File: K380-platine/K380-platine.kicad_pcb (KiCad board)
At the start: 2 copper layers, 98 x 35 mm, 0 parts

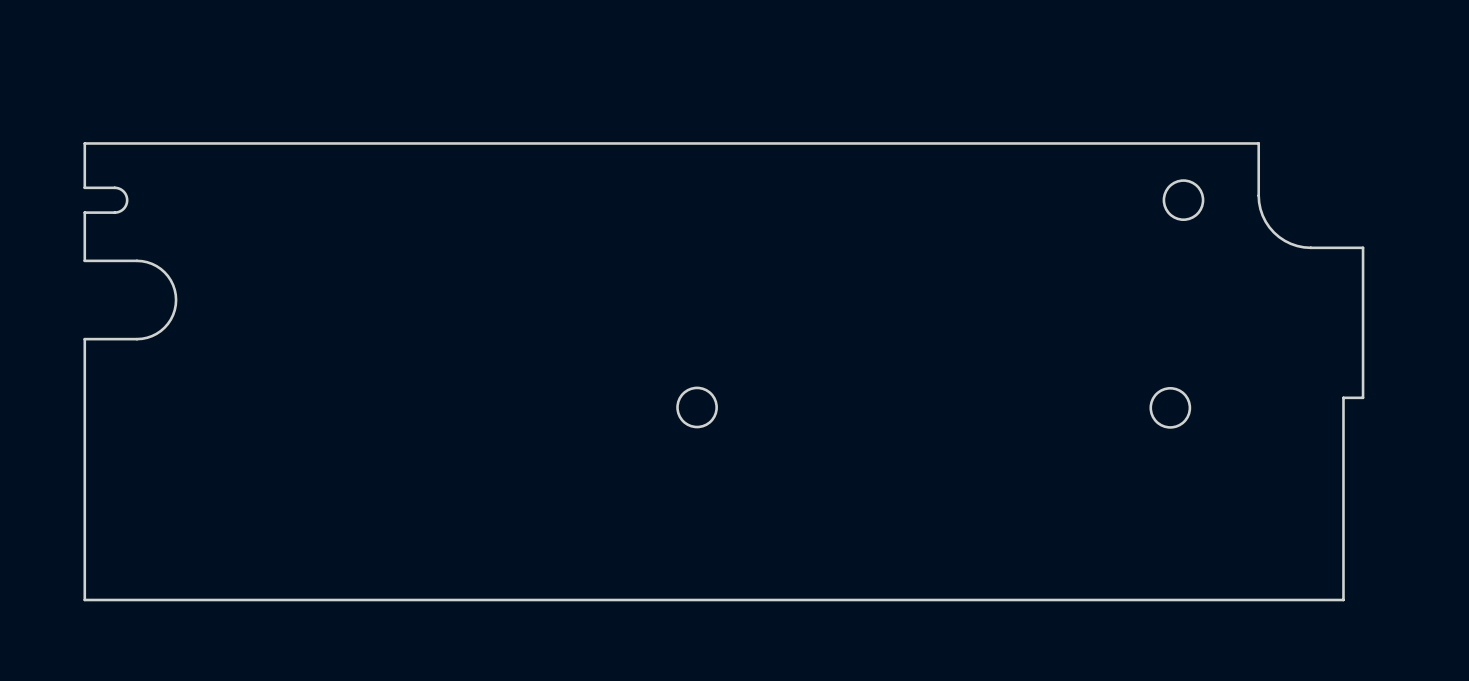
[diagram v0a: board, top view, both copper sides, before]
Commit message: Add few major components
- completely unconnected
- created schematic for M.2 sparkfun nRF52840 module
- included SparkFun footprint library
- position a few major components on the footprint
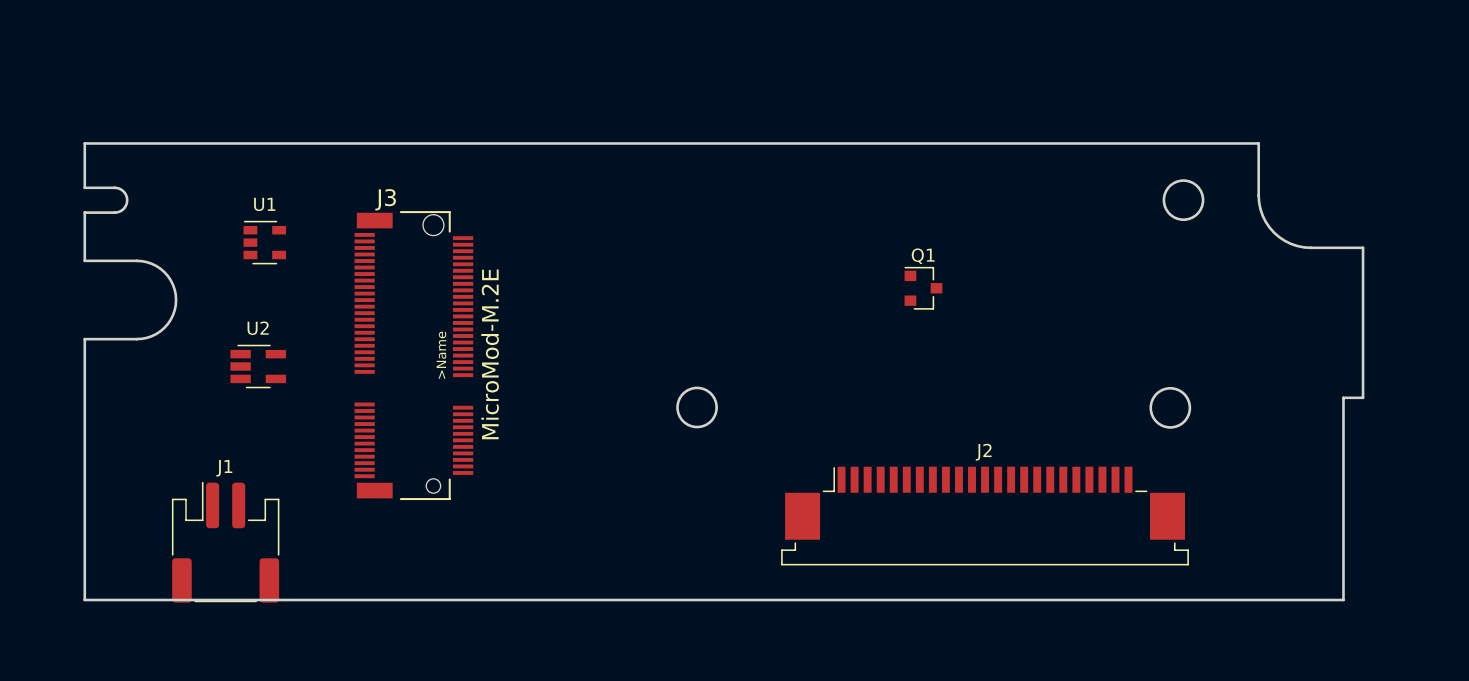
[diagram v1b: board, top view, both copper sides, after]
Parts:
- added J1: JST-PH 2, Connector_JST:JST_PH_S2B-PH-SM4-TB_1x02-1MP_P2.00mm_Horizontal, F.Cu at (86.5, 96.0)
- added J2: Conn_01x23, Connector_FFC-FPC:TE_2-84952-3_1x23-1MP_P1.0mm_Horizontal, F.Cu at (144.7, 93.0)
- added J3: MicroMod-M.2E, SparkFun MicroMod:M.2-CONNECTOR-E, F.Cu at (102.4, 81.7)
- added Q1: PMost Enc FET -20V, Package_TO_SOT_SMD:SOT-23, F.Cu at (140.0, 76.5)
- added U1: XC6220B331MR, Package_TO_SOT_SMD:SOT-23-5, F.Cu at (89.5, 73.0)
- added U2: MCP73831-2-OT, Package_TO_SOT_SMD:SOT-23-5_HandSoldering, F.Cu at (89.0, 82.5)

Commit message: Basic sorting of components on footprint
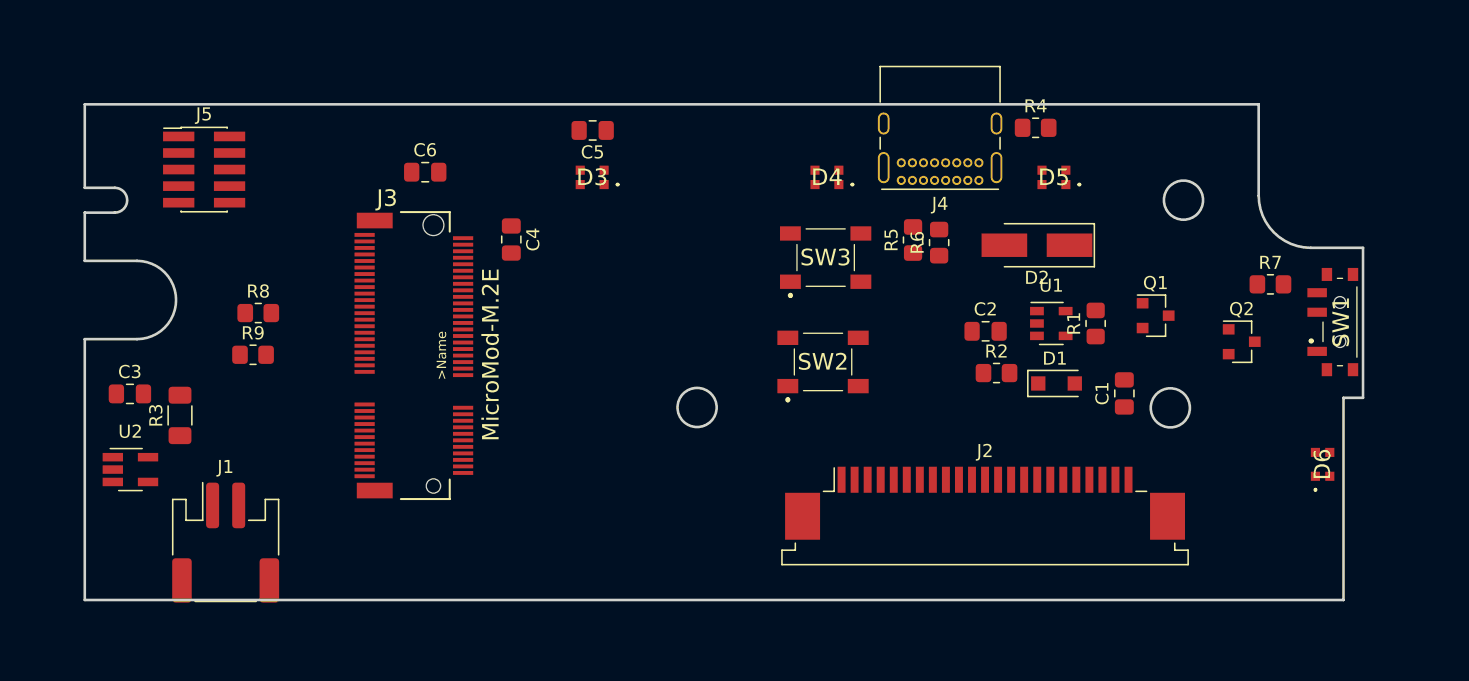
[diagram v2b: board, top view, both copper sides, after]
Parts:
- added C1: 10uF, Capacitor_SMD:C_0805_2012Metric_Pad1.18x1.45mm_HandSolder, F.Cu at (155.4, 84.6)
- added C2: 4.7uF, Capacitor_SMD:C_0805_2012Metric_Pad1.18x1.45mm_HandSolder, F.Cu at (144.8, 79.8)
- added C3: 10uF, Capacitor_SMD:C_0805_2012Metric_Pad1.18x1.45mm_HandSolder, F.Cu at (79.2, 84.6)
- added C4: 10uF, Capacitor_SMD:C_0805_2012Metric_Pad1.18x1.45mm_HandSolder, F.Cu at (108.4, 72.8)
- added C5: 0.1uF, Capacitor_SMD:C_0805_2012Metric_Pad1.18x1.45mm_HandSolder, F.Cu at (114.6, 64.4)
- added C6: 0.1uF, Capacitor_SMD:C_0805_2012Metric_Pad1.18x1.45mm_HandSolder, F.Cu at (101.8, 67.6)
- added D1: MBR1020VL, Diode_SMD:D_SOD-123F, F.Cu at (150.2, 83.8)
- added D2: TVS 5V, Diode_SMD:D_SMA_Handsoldering, F.Cu at (148.7, 73.2)
- added D3: WS2812B, LibraryLoader:WS28122020, F.Cu at (114.6, 68.0)
- added D4: WS2812B, LibraryLoader:WS28122020, F.Cu at (132.6, 68.0)
- added D5: WS2812B, LibraryLoader:WS28122020, F.Cu at (150.0, 68.0)
- added D6: WS2812B, LibraryLoader:WS28122020, F.Cu at (170.6, 90.0)
- added J4: USB_C_Receptacle_USB2.0, Connector_USB:USB_C_Receptacle_GCT_USB4085, F.Cu at (144.2, 68.2)
- added J5: Conn_ARM_JTAG_SWD_10, Connector_PinHeader_1.27mm:PinHeader_2x05_P1.27mm_Vertical_SMD, F.Cu at (84.8, 67.4)
- added Q2: Q_NMOS_DGS, Package_TO_SOT_SMD:SOT-23, F.Cu at (164.4, 80.6)
- added R1: 100K, Resistor_SMD:R_0805_2012Metric_Pad1.20x1.40mm_HandSolder, F.Cu at (153.2, 79.2)
- added R2: 100K, Resistor_SMD:R_0805_2012Metric_Pad1.20x1.40mm_HandSolder, F.Cu at (145.6, 83.0)
- added R3: RProg, Resistor_SMD:R_1206_3216Metric_Pad1.30x1.75mm_HandSolder, F.Cu at (83.0, 86.2)
- added R4: 1M, Resistor_SMD:R_0805_2012Metric_Pad1.20x1.40mm_HandSolder, F.Cu at (148.6, 64.2)
- added R5: 5.1k 20%, Resistor_SMD:R_0805_2012Metric_Pad1.20x1.40mm_HandSolder, F.Cu at (139.2, 72.8)
- added R6: 5.1k 20%, Resistor_SMD:R_0805_2012Metric_Pad1.20x1.40mm_HandSolder, F.Cu at (141.2, 73.0)
- added R7: 100K, Resistor_SMD:R_0805_2012Metric_Pad1.20x1.40mm_HandSolder, F.Cu at (166.6, 76.2)
- added R8: 100K, Resistor_SMD:R_0805_2012Metric_Pad1.20x1.40mm_HandSolder, F.Cu at (89.0, 78.4)
- added R9: 100K, Resistor_SMD:R_0805_2012Metric_Pad1.20x1.40mm_HandSolder, F.Cu at (88.6, 81.6)
- added SW1: EG1215AA, LibraryLoader:EG1215AA, F.Cu at (171.9, 79.1)
- added SW2: SW_Push, LibraryLoader:MJTP1140AAUTR, F.Cu at (132.3, 82.2)
- added SW3: SW_Push, LibraryLoader:MJTP1140AAUTR, F.Cu at (132.5, 74.2)
- moved U1 60.6 mm to (149.8, 79.2)
- moved Q1 17.9 mm to (157.8, 78.6)
- moved U2 12.6 mm to (79.2, 90.4)
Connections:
- net Net-(J3-Pad13) renamed CSTAT
- net Net-(U2-Pad1) renamed CStat
- J1 pad 1: Net-(J1-Pad1) -> GND
- J1 pad 2: Net-(J1-Pad2) -> VBAT
- J2 pad 1: Net-(J2-Pad1) -> COL1
- J2 pad 10: Net-(J2-Pad10) -> COL2
- J2 pad 11: Net-(J2-Pad11) -> COL3
- J2 pad 12: Net-(J2-Pad12) -> COL4
- J2 pad 13: Net-(J2-Pad13) -> COL5
- J2 pad 14: Net-(J2-Pad14) -> COL6
- J2 pad 15: Net-(J2-Pad15) -> COL7
- J2 pad 16: Net-(J2-Pad16) -> COL8
- J2 pad 17: Net-(J2-Pad17) -> COL9
- J2 pad 18: Net-(J2-Pad18) -> COL10
- J2 pad 19: Net-(J2-Pad19) -> COL11
- J2 pad 2: Net-(J2-Pad2) -> ROW1
- J2 pad 20: Net-(J2-Pad20) -> COL12
- J2 pad 21: Net-(J2-Pad21) -> COL13
- J2 pad 22: Net-(J2-Pad22) -> COL14
- J2 pad 23: Net-(J2-Pad23) -> COL15
- J2 pad 3: Net-(J2-Pad3) -> ROW2
- J2 pad 4: Net-(J2-Pad4) -> ROW3
- J2 pad 5: Net-(J2-Pad5) -> ROW4
- J2 pad 6: Net-(J2-Pad6) -> ROW5
- J2 pad 7: Net-(J2-Pad7) -> ROW6
- J2 pad 8: Net-(J2-Pad8) -> ROW7
- J2 pad 9: Net-(J2-Pad9) -> ROW8
- J3 pad 1: Net-(J3-Pad1) -> GND
- J3 pad 10: Net-(J3-Pad10) -> COL13
- J3 pad 11: Net-(J3-Pad11) -> BOOT
- J3 pad 12: Net-(J3-Pad12) -> COL2
- J3 pad 14: Net-(J3-Pad14) -> COL5
- J3 pad 15: Net-(J3-Pad15) -> ROW6
- J3 pad 16: Net-(J3-Pad16) -> COL6
- J3 pad 18: Net-(J3-Pad18) -> ROW5
- J3 pad 19: Net-(J3-Pad19) -> ROW7
- J3 pad 2: Net-(J3-Pad2) -> V3.3
- J3 pad 20: Net-(J3-Pad20) -> ROW2
- J3 pad 21: Net-(J3-Pad21) -> SWDCLK
- J3 pad 22: Net-(J3-Pad22) -> ROW4
- J3 pad 23: Net-(J3-Pad23) -> SWDIO
- J3 pad 3: Net-(J3-Pad3) -> D+
- J3 pad 32: Net-(J3-Pad32) -> COL1
- J3 pad 33: Net-(J3-Pad33) -> GND
- J3 pad 36: Net-(J3-Pad36) -> GND
- J3 pad 39: Net-(J3-Pad39) -> GND
- J3 pad 4: Net-(J3-Pad4) -> V3.3
- J3 pad 40: Net-(J3-Pad40) -> COL15
- J3 pad 45: Net-(J3-Pad45) -> GND
- J3 pad 47: Net-(J3-Pad47) -> COL7
- J3 pad 48: Net-(J3-Pad48) -> ROW8
- J3 pad 5: Net-(J3-Pad5) -> D-
- J3 pad 50: Net-(J3-Pad50) -> COL11
- J3 pad 51: Net-(J3-Pad51) -> DLED
- J3 pad 52: Net-(J3-Pad52) -> COL12
- J3 pad 53: Net-(J3-Pad53) -> COL10
- J3 pad 55: Net-(J3-Pad55) -> COL9
- J3 pad 57: Net-(J3-Pad57) -> COL14
- J3 pad 6: Net-(J3-Pad6) -> RESET
- J3 pad 61: Net-(J3-Pad61) -> VDIV
- J3 pad 63: Net-(J3-Pad63) -> COL4
- J3 pad 65: Net-(J3-Pad65) -> COL3
- J3 pad 69: Net-(J3-Pad69) -> ROW1
- J3 pad 7: Net-(J3-Pad7) -> GND
- J3 pad 71: Net-(J3-Pad71) -> ROW3
- J3 pad 73: Net-(J3-Pad73) -> COL8
- J3 pad 74: Net-(J3-Pad74) -> V3.3
- J3 pad 75: Net-(J3-Pad75) -> GND
- J3 pad 9: Net-(J3-Pad9) -> VUSB
- Q1 pad 1: Net-(Q1-Pad1) -> VUSB
- Q1 pad 2: Net-(Q1-Pad2) -> Net-(C1-Pad1)
- U1 pad 1: Net-(U1-Pad1) -> Net-(C1-Pad1)
- U1 pad 2: Net-(U1-Pad2) -> GND
- U1 pad 5: Net-(U1-Pad5) -> V3.3
- U2 pad 2: Net-(U2-Pad2) -> GND
- U2 pad 3: Net-(U2-Pad3) -> VBAT
- U2 pad 4: Net-(U2-Pad4) -> VUSB
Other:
- board size 98 x 35 mm -> 98 x 38 mm

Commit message: Reordered keyboard matrix pins
- layout traces isn't as random as before
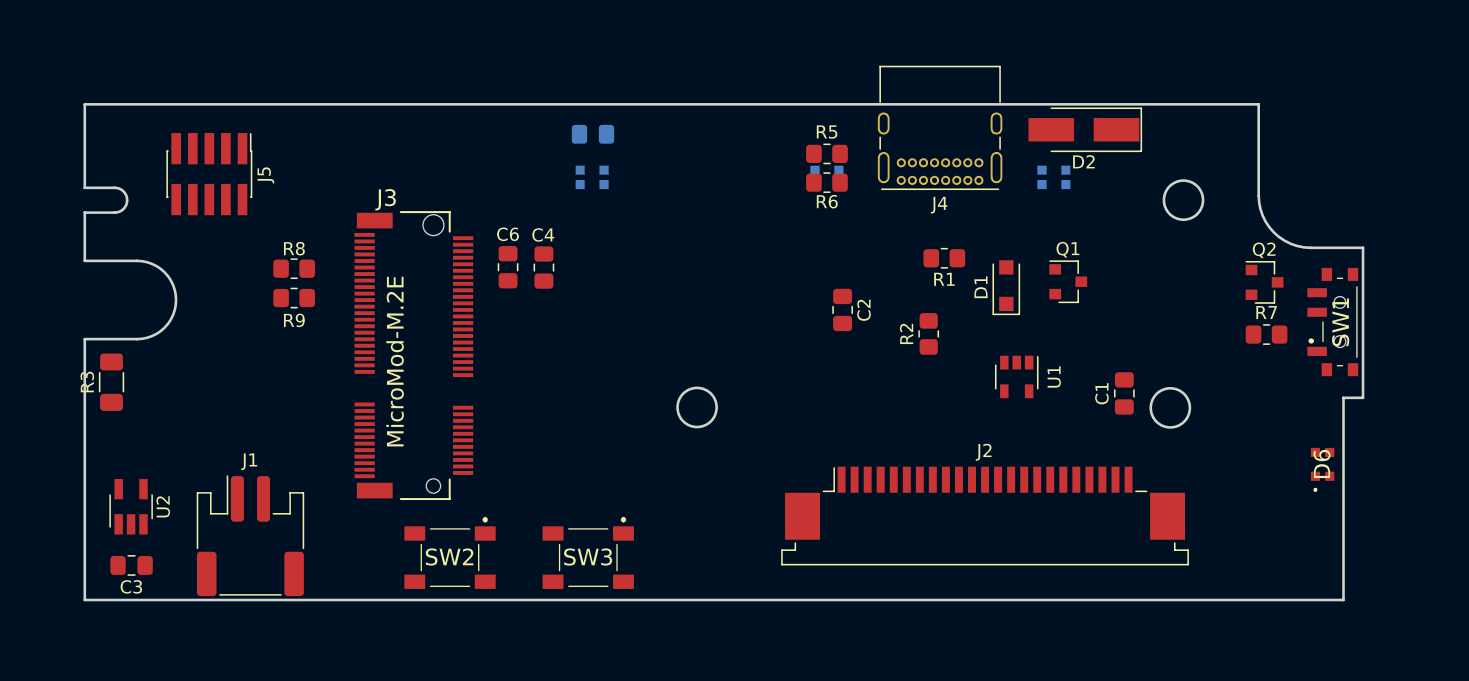
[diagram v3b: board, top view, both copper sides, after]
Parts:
- removed R4: 1M, Resistor_SMD:R_0805_2012Metric_Pad1.20x1.40mm_HandSolder
- C5, D3, D4, D5: moved to B.Cu
- moved SW2 32.3 mm to (103.7, 97.2), turned to 180 degrees
- moved SW3 29.3 mm to (114.3, 97.2), turned to 180 degrees
- moved C3 13.2 mm to (79.3, 97.8), turned to 180 degrees
- moved R1 12.6 mm to (141.6, 74.2), turned to 180 degrees
- moved C2 11.1 mm to (133.8, 78.2), turned to 270 degrees
- moved R6 9.75 mm to (132.6, 68.4), turned to 0 degrees
- moved C6 9.67 mm to (108.2, 74.9), turned to 270 degrees
- moved D2 9.55 mm to (152.3, 64.3)
- moved R5 9.33 mm to (132.6, 66.2), turned to 0 degrees
- moved D1 8.43 mm to (146.3, 76.3), turned to 90 degrees
- moved R9 7.31 mm to (91.8, 75.0), turned to 180 degrees
- moved Q1 7.19 mm to (151.1, 76.0)
- moved R2 6.00 mm to (140.4, 80.0), turned to 90 degrees
- moved R3 5.84 mm to (77.8, 83.7)
- moved U1 4.88 mm to (147.2, 83.3), turned to 270 degrees
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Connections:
- J3 pad 10: COL13 -> COL1
- J3 pad 14: COL5 -> COL3
- J3 pad 15: ROW6 -> Net-(J3-Pad15)
- J3 pad 16: COL6 -> COL4
- J3 pad 18: ROW5 -> COL5
- J3 pad 19: ROW7 -> Net-(J3-Pad19)
- J3 pad 20: ROW2 -> COL6
- J3 pad 22: ROW4 -> COL7
- J3 pad 32: COL1 -> COL8
- J3 pad 34: Net-(J3-Pad34) -> COL9
- J3 pad 38: Net-(J3-Pad38) -> COL10
- J3 pad 40: COL15 -> COL11
- J3 pad 42: Net-(J3-Pad42) -> COL12
- J3 pad 44: Net-(J3-Pad44) -> COL13
- J3 pad 46: Net-(J3-Pad46) -> COL14
- J3 pad 47: COL7 -> Net-(J3-Pad47)
- J3 pad 48: ROW8 -> COL15
- J3 pad 49: Net-(J3-Pad49) -> VDIV
- J3 pad 50: COL11 -> Net-(J3-Pad50)
- J3 pad 52: COL12 -> Net-(J3-Pad52)
- J3 pad 53: COL10 -> Net-(J3-Pad53)
- J3 pad 55: COL9 -> Net-(J3-Pad55)
- J3 pad 57: COL14 -> Net-(J3-Pad57)
- J3 pad 59: Net-(J3-Pad59) -> ROW8
- J3 pad 61: VDIV -> ROW7
- J3 pad 63: COL4 -> ROW6
- J3 pad 65: COL3 -> ROW5
- J3 pad 67: Net-(J3-Pad67) -> ROW4
- J3 pad 69: ROW1 -> ROW3
- J3 pad 71: ROW3 -> ROW2
- J3 pad 73: COL8 -> ROW1

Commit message: Finished basic layout
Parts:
- moved C1 21.4 mm to (135.5, 76.6), turned to 180 degrees
- moved R2 18.0 mm to (158.3, 78.2), turned to 0 degrees
- moved Q2 16.0 mm to (150.4, 79.1)
- moved C6 16.0 mm to (109.1, 90.8)
- moved C4 15.9 mm to (111.5, 90.8)
- moved U1 11.4 mm to (135.8, 82.4), turned to 180 degrees
- moved R7 8.91 mm to (158.3, 76.2)
- moved R1 6.06 mm to (135.6, 74.5)
- moved D1 4.37 mm to (142.1, 75.5)
- moved D2 3.61 mm to (152.6, 68.0)
- moved C2 3.12 mm to (130.9, 79.4), turned to 90 degrees
- moved SW2 1.15 mm to (102.5, 97.2), turned to 0 degrees
- moved Q1 0.99 mm to (150.4, 75.3)
- moved SW3 0.85 mm to (113.5, 97.2)
- moved R3 0.36 mm to (78.0, 83.9)
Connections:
- Q2 pad 2: Net-(Q2-Pad2) -> VBAT
- Q2 pad 3: VBAT -> Net-(Q2-Pad3)
- R7 pad 1: Net-(Q2-Pad2) -> Net-(Q2-Pad3)

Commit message: Change pin of DLED and CSTAT
- cstat was misspelled so KiCad made no connection
- DLED is closer to where it needs to be
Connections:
- J3 pad 51: DLED -> Net-(J3-Pad51)
- J3 pad 52: Net-(J3-Pad52) -> DLED
- U2 pad 1: CStat -> CSTAT
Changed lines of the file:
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@@
     (zones 0)
     (modules 32)
-    (nets 72)
+    (nets 71)
   )
   (page A4)
@@
     (pad_to_mask_clearance 0)
     (aux_axis_origin 0 0)
-    (visible_elements FFFFF77F)
+    (visible_elements FFFFFF7F)
     (pcbplotparams
       (layerselection 0x010fc_ffffffff)
@@
   (net 10 "Net-(J3-Pad55)")
   (net 11 "Net-(J3-Pad53)")
-  (net 12 "Net-(J3-Pad52)")
+  (net 12 "Net-(J3-Pad51)")
   (net 13 "Net-(J3-Pad50)")
   (net 14 "Net-(J3-Pad47)")
@@
   (net 66 "Net-(J4-PadB5)")
   (net 67 "Net-(R7-Pad2)")
-  (net 68 CStat)
-  (net 69 "Net-(J4-PadB8)")
-  (net 70 "Net-(J4-PadA8)")
-  (net 71 "Net-(Q2-Pad3)")
+  (net 68 "Net-(J4-PadB8)")
+  (net 69 "Net-(J4-PadA8)")
+  (net 70 "Net-(Q2-Pad3)")
   (net_class Default "This is the default net class."
     (clearance 0.2)
@@
     (add_net COL9)
     (add_net CSTAT)
-    (add_net CStat)
     (add_net D+)
     (add_net D-)
@@
     (add_net "Net-(J3-Pad47)")
     (add_net "Net-(J3-Pad50)")
-    (add_net "Net-(J3-Pad52)")
+    (add_net "Net-(J3-Pad51)")
     (add_net "Net-(J3-Pad53)")
     (add_net "Net-(J3-Pad55)")
@@
       (net 18 GND))
     (pad B8 thru_hole circle (at 1.7 1.35 180) (size 0.7 0.7) (drill 0.4) (layers *.Cu *.Mask)
-      (net 69 "Net-(J4-PadB8)"))
+      (net 68 "Net-(J4-PadB8)"))
     (pad B7 thru_hole circle (at 2.55 1.35 180) (size 0.7 0.7) (drill 0.4) (layers *.Cu *.Mask)
       (net 57 D-))
@@
       (net 22 VUSB))
     (pad A8 thru_hole circle (at 4.25 0 180) (size 0.7 0.7) (drill 0.4) (layers *.Cu *.Mask)
-      (net 70 "Net-(J4-PadA8)"))
+      (net 69 "Net-(J4-PadA8)"))
     (pad A7 thru_hole circle (at 3.4 0 180) (size 0.7 0.7) (drill 0.4) (layers *.Cu *.Mask)
       (net 57 D-))
@@
       (net 67 "Net-(R7-Pad2)"))
     (pad 1 smd roundrect (at -1 0) (size 1.2 1.4) (layers F.Cu F.Paste F.Mask) (roundrect_rratio 0.208333)
-      (net 71 "Net-(Q2-Pad3)"))
+      (net 70 "Net-(Q2-Pad3)"))
     (model ${KISYS3DMOD}/Resistor_SMD.3dshapes/R_0805_2012Metric.wrl
       (at (xyz 0 0 0))
@@
     (fp_line (start 0.76 1.58) (end -0.7 1.58) (layer F.SilkS) (width 0.12))
     (pad 3 smd rect (at 1 0) (size 0.9 0.8) (layers F.Cu F.Paste F.Mask)
-      (net 71 "Net-(Q2-Pad3)"))
+      (net 70 "Net-(Q2-Pad3)"))
     (pad 2 smd rect (at -1 0.95) (size 0.9 0.8) (layers F.Cu F.Paste F.Mask)
       (net 21 VBAT))
@@
       (net 11 "Net-(J3-Pad53)") (solder_mask_margin 0.1016))
     (pad 52 smd rect (at -3.5 -2.275 90) (size 0.3 1.55) (layers F.Cu F.Mask)
-      (net 12 "Net-(J3-Pad52)") (solder_mask_margin 0.1016))
+      (net 23 DLED) (solder_mask_margin 0.1016))
     (pad 51 smd rect (at -3.25 5.275 90) (size 0.3 1.55) (layers F.Cu F.Mask)
-      (net 23 DLED) (solder_mask_margin 0.1016))
+      (net 12 "Net-(J3-Pad51)") (solder_mask_margin 0.1016))
     (pad 50 smd rect (at -3 -2.275 90) (size 0.3 1.55) (layers F.Cu F.Mask)
       (net 13 "Net-(J3-Pad50)") (solder_mask_margin 0.1016))
@@
       (net 18 GND))
     (pad 1 smd rect (at -1.35 -0.95 90) (size 1.56 0.65) (layers F.Cu F.Paste F.Mask)
-      (net 68 CStat))
+      (net 54 CSTAT))
     (model ${KISYS3DMOD}/Package_TO_SOT_SMD.3dshapes/SOT-23-5.wrl
       (at (xyz 0 0 0))
